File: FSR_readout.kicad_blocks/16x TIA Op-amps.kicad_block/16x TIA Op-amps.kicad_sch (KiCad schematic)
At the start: 46 parts, among them U18 TLV9064, U19 TLV9064, U20 TLV9064, U3 TLV9064

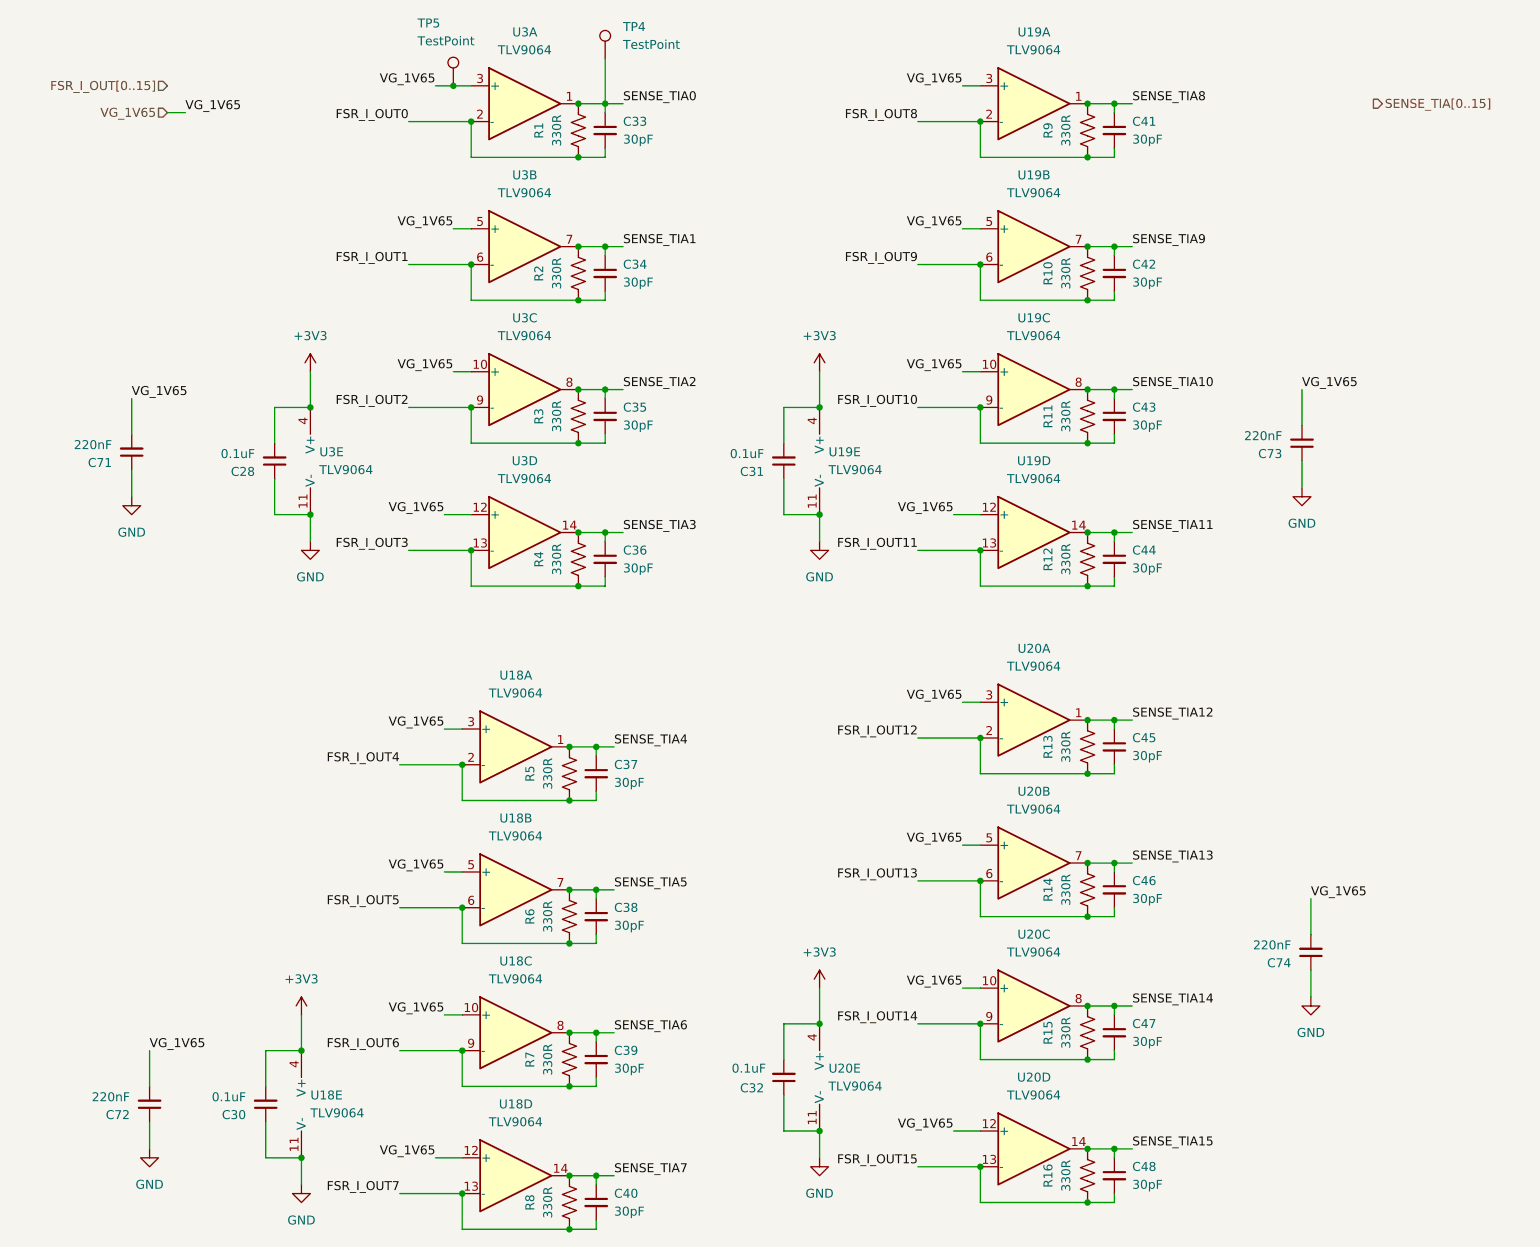
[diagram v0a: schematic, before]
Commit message: adjust VG issue for internal ADC version; changed naming for VG
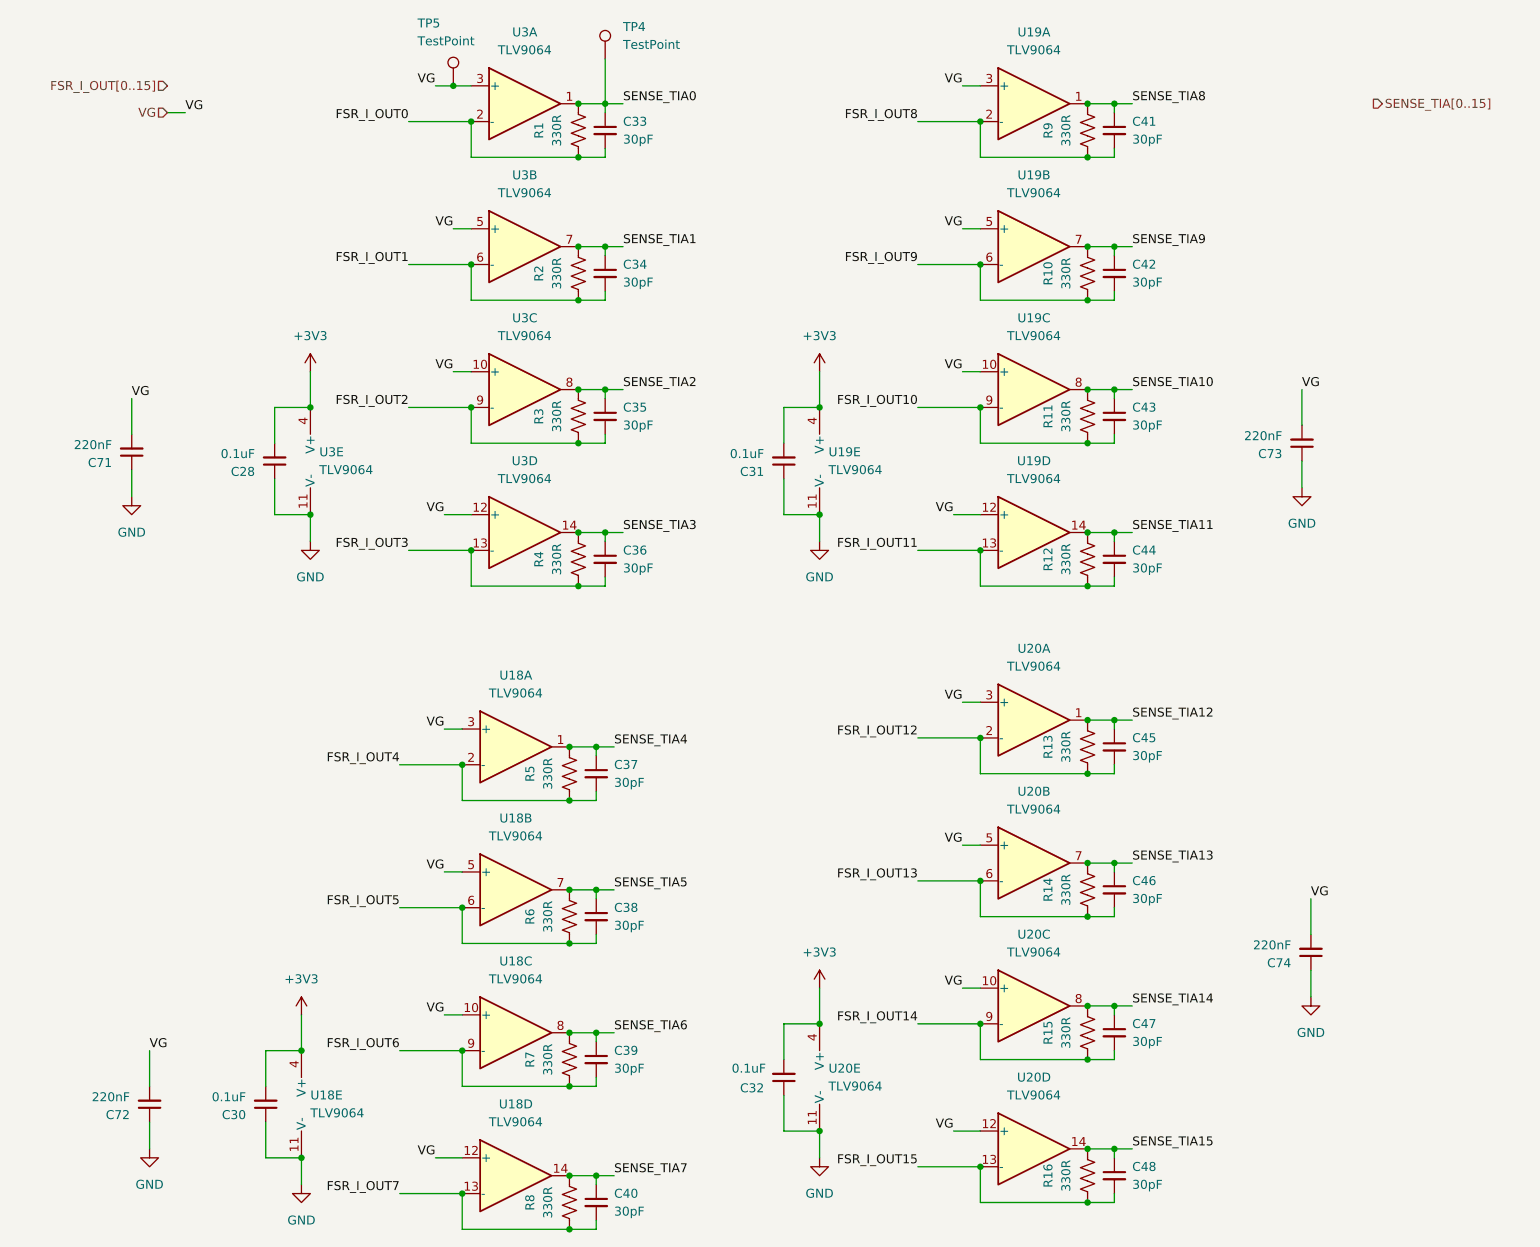
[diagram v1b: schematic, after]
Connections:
- net VG_1V65 renamed VG
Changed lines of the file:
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@@
 		)
 	)
-	(label "VG_1V65"
+	(label "VG"
 		(at 38.1 33.02 0)
 		(effects
@@
 		)
 	)
-	(label "VG_1V65"
+	(label "VG"
 		(at 76.2 69.85 180)
 		(effects
@@
 		)
 	)
-	(label "VG_1V65"
+	(label "VG"
 		(at 148.59 29.21 180)
 		(effects
@@
 		)
 	)
-	(label "VG_1V65"
+	(label "VG"
 		(at 148.59 49.53 180)
 		(effects
@@
 		)
 	)
-	(label "VG_1V65"
+	(label "VG"
 		(at 76.2 49.53 180)
 		(effects
@@
 		)
 	)
-	(label "VG_1V65"
+	(label "VG"
 		(at 147.32 90.17 180)
 		(effects
@@
 		)
 	)
-	(label "VG_1V65"
+	(label "VG"
 		(at 74.93 90.17 180)
 		(effects
@@
 		)
 	)
-	(label "VG_1V65"
+	(label "VG"
 		(at 147.32 177.8 180)
 		(effects
@@
 		)
 	)
-	(label "VG_1V65"
+	(label "VG"
 		(at 148.59 116.84 180)
 		(effects
@@
 		)
 	)
-	(label "VG_1V65"
+	(label "VG"
 		(at 74.93 120.65 180)
 		(effects
@@
 		)
 	)
-	(label "VG_1V65"
+	(label "VG"
 		(at 73.66 181.61 180)
 		(effects
@@
 		)
 	)
-	(label "VG_1V65"
+	(label "VG"
 		(at 196.85 72.39 0)
 		(effects
@@
 		)
 	)
-	(label "VG_1V65"
+	(label "VG"
 		(at 74.93 140.97 180)
 		(effects
@@
 		)
 	)
-	(label "VG_1V65"
+	(label "VG"
 		(at 30.48 73.66 0)
 		(effects
@@
 		)
 	)
-	(label "VG_1V65"
+	(label "VG"
 		(at 198.12 144.78 0)
 		(effects
@@
 		)
 	)
-	(label "VG_1V65"
+	(label "VG"
 		(at 148.59 137.16 180)
 		(effects
@@
 		)
 	)
-	(label "VG_1V65"
+	(label "VG"
 		(at 148.59 157.48 180)
 		(effects
@@
 		)
 	)
-	(label "VG_1V65"
+	(label "VG"
 		(at 73.66 29.21 180)
 		(effects
@@
 		)
 	)
-	(label "VG_1V65"
+	(label "VG"
 		(at 74.93 161.29 180)
 		(effects
@@
 		)
 	)
-	(label "VG_1V65"
+	(label "VG"
 		(at 148.59 69.85 180)
 		(effects
@@
 		)
 	)
-	(label "VG_1V65"
+	(label "VG"
 		(at 33.02 166.37 0)
 		(effects
@@
 		)
 	)
-	(hierarchical_label "VG_1V65"
+	(hierarchical_label "VG"
 		(shape input)
 		(at 35.56 33.02 180)
